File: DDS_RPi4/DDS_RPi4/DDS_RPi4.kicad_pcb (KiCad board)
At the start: 2 copper layers, 29.2 x 52.8 mm, 35 parts, among them J1 Raspberry_Pi_2_3, J2 Conn_Coaxial, J3 Conn_Coaxial, J4 Conn_01x02_Male, J5 Conn_01x02_Male, T1 Transformer_1P_SS, U1 AD9951, U2 LM1117-1.8, U3 5x5, Y2 20M

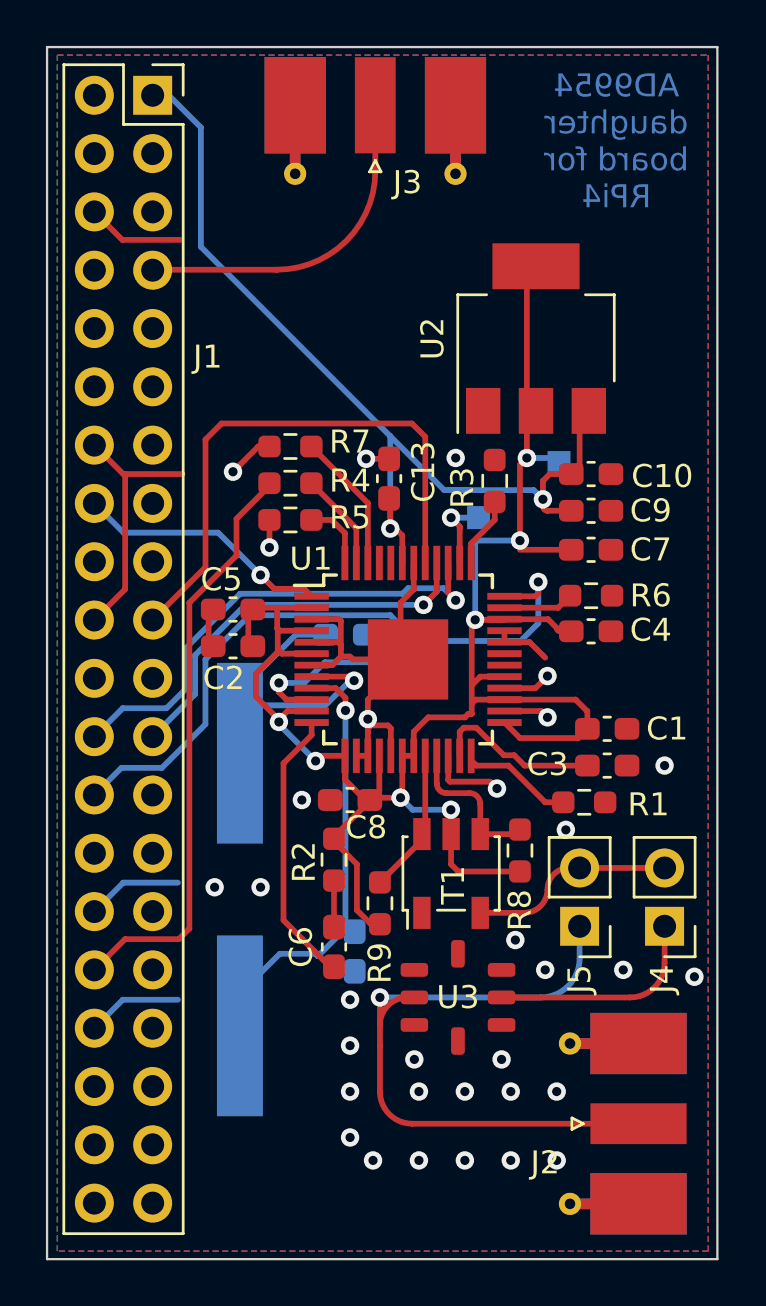
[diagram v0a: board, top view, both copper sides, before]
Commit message: update schematic and PCB (disconnect comparator out and add more decoupling capacitors)
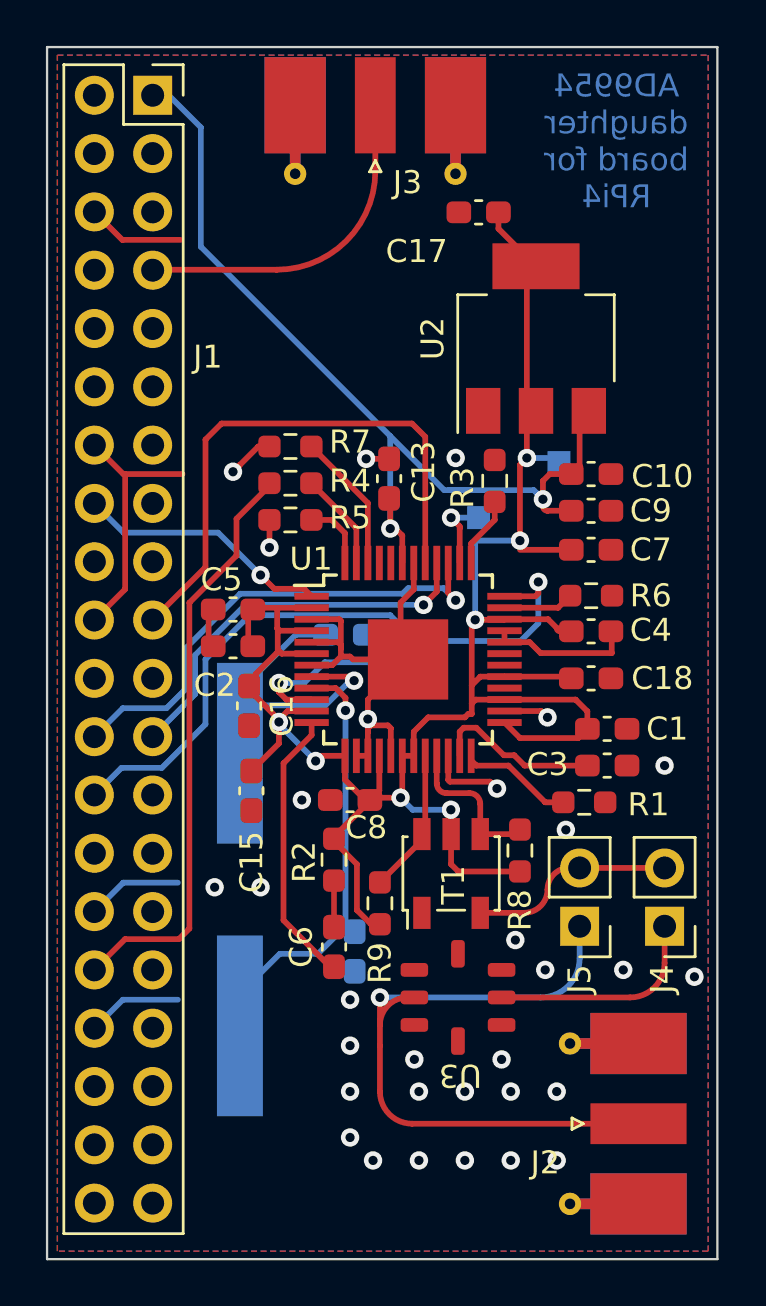
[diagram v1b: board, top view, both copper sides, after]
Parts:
- added C15: 100n, Capacitor_SMD:C_0603_1608Metric_Pad1.08x0.95mm_HandSolder, F.Cu at (133.7, 105.9)
- added C16: 100n, Capacitor_SMD:C_0603_1608Metric_Pad1.08x0.95mm_HandSolder, F.Cu at (133.6, 102.2)
- added C17: 100n, Capacitor_SMD:C_0603_1608Metric_Pad1.08x0.95mm_HandSolder, F.Cu at (143.6, 80.7)
- added C18: 100n, Capacitor_SMD:C_0603_1608Metric_Pad1.08x0.95mm_HandSolder, F.Cu at (148.5, 101.0)
- C1, C13, C4, C5, C7, C8: value C -> 100n
- C10: value C -> 4.7u
- C9: value C -> 1n
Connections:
- U1 pad 28: GND -> unconnected-(U1-Pad28)
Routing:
- net Net-(C1-Pad1): track 88.0 -> 96.9 mm
- net GND: track 64.5 -> 66.2 mm, vias 32 -> 31
